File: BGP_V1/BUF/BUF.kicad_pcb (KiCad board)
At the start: 2 copper layers, 30 x 30 mm, 23 parts, among them P1 CONN_01X05, P2 CONN_01X02, P3 CONN_01X12, U1 MC33178, U2 TLV170

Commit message: BOM for V1 BGP
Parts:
- C2, C5: footprint Capacitors_SMD:C_1206_HandSoldering -> Capacitors_Tantalum_SMD:TantalC_SizeS_EIA-3216
- moved C5 0.22 mm to (162.4, 118.6), turned to 180 degrees
- moved C2 0.10 mm to (142.0, 107.6), turned to 0 degrees
- moved C6 0.10 mm to (150.4, 114.1)
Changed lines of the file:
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@@
   (general
     (links 49)
-    (no_connects 2)
-    (area 136.924999 91.924999 167.075001 122.075001)
+    (no_connects 0)
+    (area 135.10412 91.424999 167.075001 122.779999)
     (thickness 1.6)
     (drawings 9)
@@
     )
   )
-  (module Capacitors_SMD:C_1206_HandSoldering (layer F.Cu)
-    (at 142 107.5 180)
-    (descr "Capacitor SMD 1206, hand soldering")
-    (tags "capacitor 1206")
-    (attr smd)
-    (fp_text reference C2 (at 2.8 1.5 180) (layer F.SilkS)
-      (effects (font (size 0.6 0.6) (thickness 0.15)))
-    )
-    (fp_text value 10u (at 0 2.3 180) (layer F.Fab) hide
-      (effects (font (size 0.6 0.6) (thickness 0.15)))
-    )
-    (fp_line (start -3.3 -1.15) (end 3.3 -1.15) (layer F.CrtYd) (width 0.05))
-    (fp_line (start -3.3 1.15) (end 3.3 1.15) (layer F.CrtYd) (width 0.05))
-    (fp_line (start -3.3 -1.15) (end -3.3 1.15) (layer F.CrtYd) (width 0.05))
-    (fp_line (start 3.3 -1.15) (end 3.3 1.15) (layer F.CrtYd) (width 0.05))
-    (fp_line (start 1 -1.025) (end -1 -1.025) (layer F.SilkS) (width 0.15))
-    (fp_line (start -1 1.025) (end 1 1.025) (layer F.SilkS) (width 0.15))
-    (pad 1 smd rect (at -2 0 180) (size 2 1.6) (layers F.Cu F.Paste F.Mask)
-      (net 3 "Net-(C2-Pad1)"))
-    (pad 2 smd rect (at 2 0 180) (size 2 1.6) (layers F.Cu F.Paste F.Mask)
-      (net 18 /BUF_O))
-    (model Capacitors_SMD.3dshapes/C_1206_HandSoldering.wrl
-      (at (xyz 0 0 0))
-      (scale (xyz 1 1 1))
-      (rotate (xyz 0 0 0))
-    )
-  )
   (module Capacitors_SMD:C_0805_HandSoldering (layer F.Cu)
     (at 145.3 102.9 270)
@@
       (net 8 Earth))
     (model Capacitors_SMD.3dshapes/C_0805_HandSoldering.wrl
-      (at (xyz 0 0 0))
-      (scale (xyz 1 1 1))
-      (rotate (xyz 0 0 0))
-    )
-  )
-  (module Capacitors_SMD:C_1206_HandSoldering (layer F.Cu)
-    (at 162.5 118.4)
-    (descr "Capacitor SMD 1206, hand soldering")
-    (tags "capacitor 1206")
-    (attr smd)
-    (fp_text reference C5 (at -2.9 -1.6) (layer F.SilkS)
-      (effects (font (size 0.6 0.6) (thickness 0.15)))
-    )
-    (fp_text value 10u (at 0 2.3) (layer F.Fab) hide
-      (effects (font (size 0.6 0.6) (thickness 0.15)))
-    )
-    (fp_line (start -3.3 -1.15) (end 3.3 -1.15) (layer F.CrtYd) (width 0.05))
-    (fp_line (start -3.3 1.15) (end 3.3 1.15) (layer F.CrtYd) (width 0.05))
-    (fp_line (start -3.3 -1.15) (end -3.3 1.15) (layer F.CrtYd) (width 0.05))
-    (fp_line (start 3.3 -1.15) (end 3.3 1.15) (layer F.CrtYd) (width 0.05))
-    (fp_line (start 1 -1.025) (end -1 -1.025) (layer F.SilkS) (width 0.15))
-    (fp_line (start -1 1.025) (end 1 1.025) (layer F.SilkS) (width 0.15))
-    (pad 1 smd rect (at -2 0) (size 2 1.6) (layers F.Cu F.Paste F.Mask)
-      (net 9 /OUT))
-    (pad 2 smd rect (at 2 0) (size 2 1.6) (layers F.Cu F.Paste F.Mask)
-      (net 10 "Net-(C5-Pad2)"))
-    (model Capacitors_SMD.3dshapes/C_1206_HandSoldering.wrl
       (at (xyz 0 0 0))
       (scale (xyz 1 1 1))
@@
       (net 11 /V+))
     (model ${KISYS3DMOD}/TO_SOT_Packages_SMD.3dshapes\SOT-23-5.wrl
-      (at (xyz 0 0 0))
-      (scale (xyz 1 1 1))
-      (rotate (xyz 0 0 0))
-    )
-  )
-  (module Capacitors_SMD:C_0805_HandSoldering (layer B.Cu)
-    (at 150.3 114.1)
-    (descr "Capacitor SMD 0805, hand soldering")
-    (tags "capacitor 0805")
-    (attr smd)
-    (fp_text reference C6 (at 1.7 -1.3) (layer B.SilkS)
-      (effects (font (size 0.6 0.6) (thickness 0.15)) (justify mirror))
-    )
-    (fp_text value 10u (at 0 -1.75) (layer B.Fab) hide
-      (effects (font (size 0.6 0.6) (thickness 0.15)) (justify mirror))
-    )
-    (fp_text user %R (at 1.8 -1.4) (layer B.Fab) hide
-      (effects (font (size 0.6 0.6) (thickness 0.15)) (justify mirror))
-    )
-    (fp_line (start -1 -0.62) (end -1 0.62) (layer B.Fab) (width 0.1))
-    (fp_line (start 1 -0.62) (end -1 -0.62) (layer B.Fab) (width 0.1))
-    (fp_line (start 1 0.62) (end 1 -0.62) (layer B.Fab) (width 0.1))
-    (fp_line (start -1 0.62) (end 1 0.62) (layer B.Fab) (width 0.1))
-    (fp_line (start 0.5 0.85) (end -0.5 0.85) (layer B.SilkS) (width 0.12))
-    (fp_line (start -0.5 -0.85) (end 0.5 -0.85) (layer B.SilkS) (width 0.12))
-    (fp_line (start -2.25 0.88) (end 2.25 0.88) (layer B.CrtYd) (width 0.05))
-    (fp_line (start -2.25 0.88) (end -2.25 -0.87) (layer B.CrtYd) (width 0.05))
-    (fp_line (start 2.25 -0.87) (end 2.25 0.88) (layer B.CrtYd) (width 0.05))
-    (fp_line (start 2.25 -0.87) (end -2.25 -0.87) (layer B.CrtYd) (width 0.05))
-    (pad 1 smd rect (at -1.25 0) (size 1.5 1.25) (layers B.Cu B.Paste B.Mask)
-      (net 11 /V+))
-    (pad 2 smd rect (at 1.25 0) (size 1.5 1.25) (layers B.Cu B.Paste B.Mask)
-      (net 12 /V-))
-    (model Capacitors_SMD.3dshapes/C_0805.wrl
       (at (xyz 0 0 0))
       (scale (xyz 1 1 1))
@@
       (rotate (xyz 0 0 0))
     )
+  )
+  (module Capacitors_Tantalum_SMD:TantalC_SizeS_EIA-3216 (layer F.Cu)
+    (at 142 107.6)
+    (descr "Tantal Cap. , Size S, EIA-3216, Hand Soldering")
+    (fp_text reference C2 (at -2.1 -1.4) (layer F.SilkS)
+      (effects (font (size 0.6 0.6) (thickness 0.15)))
+    )
+    (fp_text value 10u (at 0 1.27) (layer F.Fab) hide
+      (effects (font (size 0.6 0.6) (thickness 0.15)))
+    )
+    (fp_line (start 1.143 0.8128) (end 1.143 -0.8128) (layer F.SilkS) (width 0.15))
+    (fp_line (start -1.6002 -0.8128) (end -1.6002 0.8128) (layer F.SilkS) (width 0.15))
+    (fp_line (start -1.6002 0.8128) (end 1.6002 0.8128) (layer F.SilkS) (width 0.15))
+    (fp_line (start 1.6002 0.8128) (end 1.6002 -0.8128) (layer F.SilkS) (width 0.15))
+    (fp_line (start 1.6002 -0.8128) (end -1.6002 -0.8128) (layer F.SilkS) (width 0.15))
+    (pad 1 smd rect (at 1.37414 0) (size 1.95072 1.50114) (layers F.Cu F.Paste F.Mask)
+      (net 3 "Net-(C2-Pad1)"))
+    (pad 2 smd rect (at -1.37414 0) (size 1.95072 1.50114) (layers F.Cu F.Paste F.Mask)
+      (net 18 /BUF_O))
+    (model Capacitors_Tantalum_SMD.3dshapes/TantalC_SizeS_EIA-3216.wrl
+      (at (xyz 0 0 0))
+      (scale (xyz 1 1 1))
+      (rotate (xyz 0 0 0))
+    )
+  )
+  (module Capacitors_Tantalum_SMD:TantalC_SizeS_EIA-3216 (layer F.Cu)
+    (at 162.4 118.6 180)
+    (descr "Tantal Cap. , Size S, EIA-3216, Hand Soldering")
+    (fp_text reference C5 (at 2.1 1.5 180) (layer F.SilkS)
+      (effects (font (size 0.6 0.6) (thickness 0.15)))
+    )
+    (fp_text value 10u (at 0 1.27 180) (layer F.Fab) hide
+      (effects (font (size 0.6 0.6) (thickness 0.15)))
+    )
+    (fp_line (start 1.143 0.8128) (end 1.143 -0.8128) (layer F.SilkS) (width 0.15))
+    (fp_line (start -1.6002 -0.8128) (end -1.6002 0.8128) (layer F.SilkS) (width 0.15))
+    (fp_line (start -1.6002 0.8128) (end 1.6002 0.8128) (layer F.SilkS) (width 0.15))
+    (fp_line (start 1.6002 0.8128) (end 1.6002 -0.8128) (layer F.SilkS) (width 0.15))
+    (fp_line (start 1.6002 -0.8128) (end -1.6002 -0.8128) (layer F.SilkS) (width 0.15))
+    (pad 1 smd rect (at 1.37414 0 180) (size 1.95072 1.50114) (layers F.Cu F.Paste F.Mask)
+      (net 9 /OUT))
+    (pad 2 smd rect (at -1.37414 0 180) (size 1.95072 1.50114) (layers F.Cu F.Paste F.Mask)
+      (net 10 "Net-(C5-Pad2)"))
+    (model Capacitors_Tantalum_SMD.3dshapes/TantalC_SizeS_EIA-3216.wrl
+      (at (xyz 0 0 0))
+      (scale (xyz 1 1 1))
+      (rotate (xyz 0 0 0))
+    )
+  )
+  (module Capacitors_SMD:C_0805_HandSoldering (layer B.Cu)
+    (at 150.4 114.1)
+    (descr "Capacitor SMD 0805, hand soldering")
+    (tags "capacitor 0805")
+    (attr smd)
+    (fp_text reference C6 (at 1.8 -1.4) (layer B.SilkS)
+      (effects (font (size 0.6 0.6) (thickness 0.15)) (justify mirror))
+    )
+    (fp_text value 10u (at 0 -2.1) (layer B.Fab) hide
+      (effects (font (size 0.6 0.6) (thickness 0.15)) (justify mirror))
+    )
+    (fp_line (start -2.3 1) (end 2.3 1) (layer B.CrtYd) (width 0.05))
+    (fp_line (start -2.3 -1) (end 2.3 -1) (layer B.CrtYd) (width 0.05))
+    (fp_line (start -2.3 1) (end -2.3 -1) (layer B.CrtYd) (width 0.05))
+    (fp_line (start 2.3 1) (end 2.3 -1) (layer B.CrtYd) (width 0.05))
+    (fp_line (start 0.5 0.85) (end -0.5 0.85) (layer B.SilkS) (width 0.15))
+    (fp_line (start -0.5 -0.85) (end 0.5 -0.85) (layer B.SilkS) (width 0.15))
+    (pad 1 smd rect (at -1.25 0) (size 1.5 1.25) (layers B.Cu B.Paste B.Mask)
+      (net 11 /V+))
+    (pad 2 smd rect (at 1.25 0) (size 1.5 1.25) (layers B.Cu B.Paste B.Mask)
+      (net 12 /V-))
+    (model Capacitors_SMD.3dshapes/C_0805_HandSoldering.wrl
+      (at (xyz 0 0 0))
+      (scale (xyz 1 1 1))
+      (rotate (xyz 0 0 0))
+    )

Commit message: some cleanup
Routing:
- net /VF2_2: track 12.8 -> 14.1 mm
- net Earth: track 10.1 -> 9.51 mm

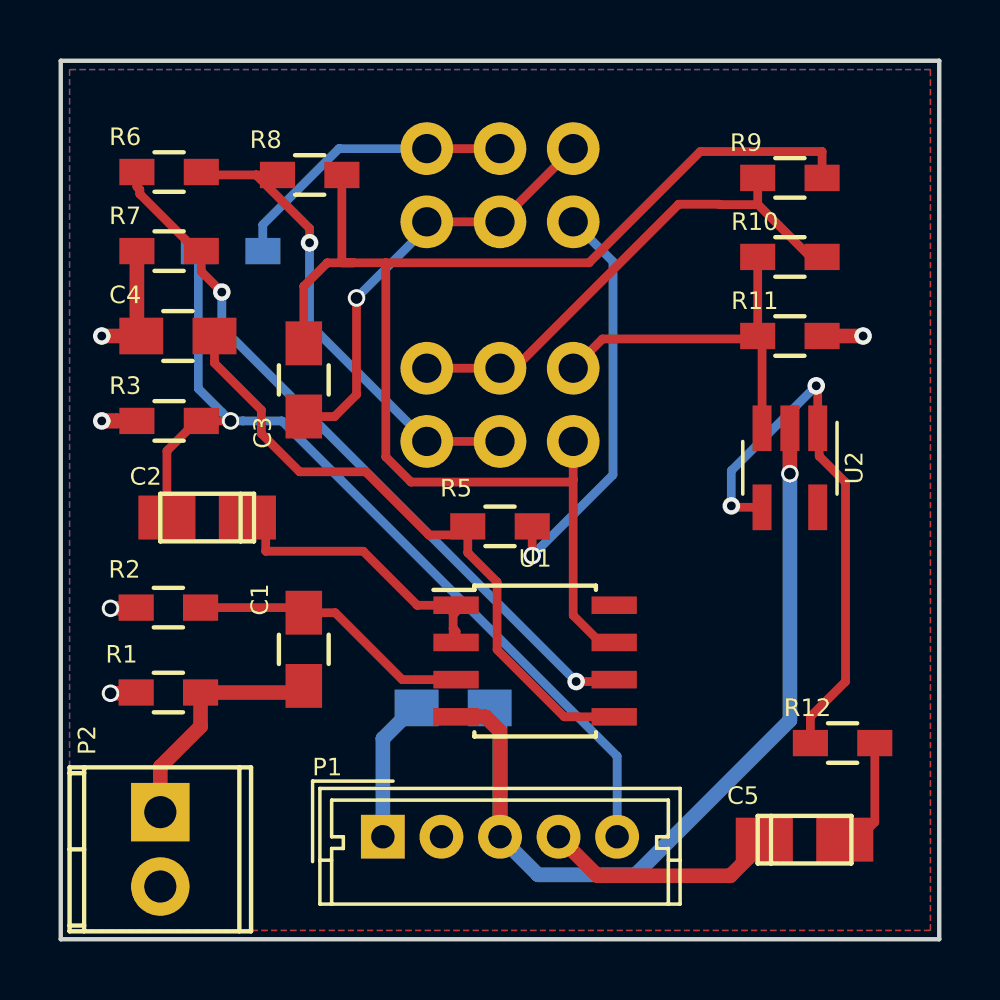
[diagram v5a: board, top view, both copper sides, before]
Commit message: Slight changes to Port layer placement - gerbers done
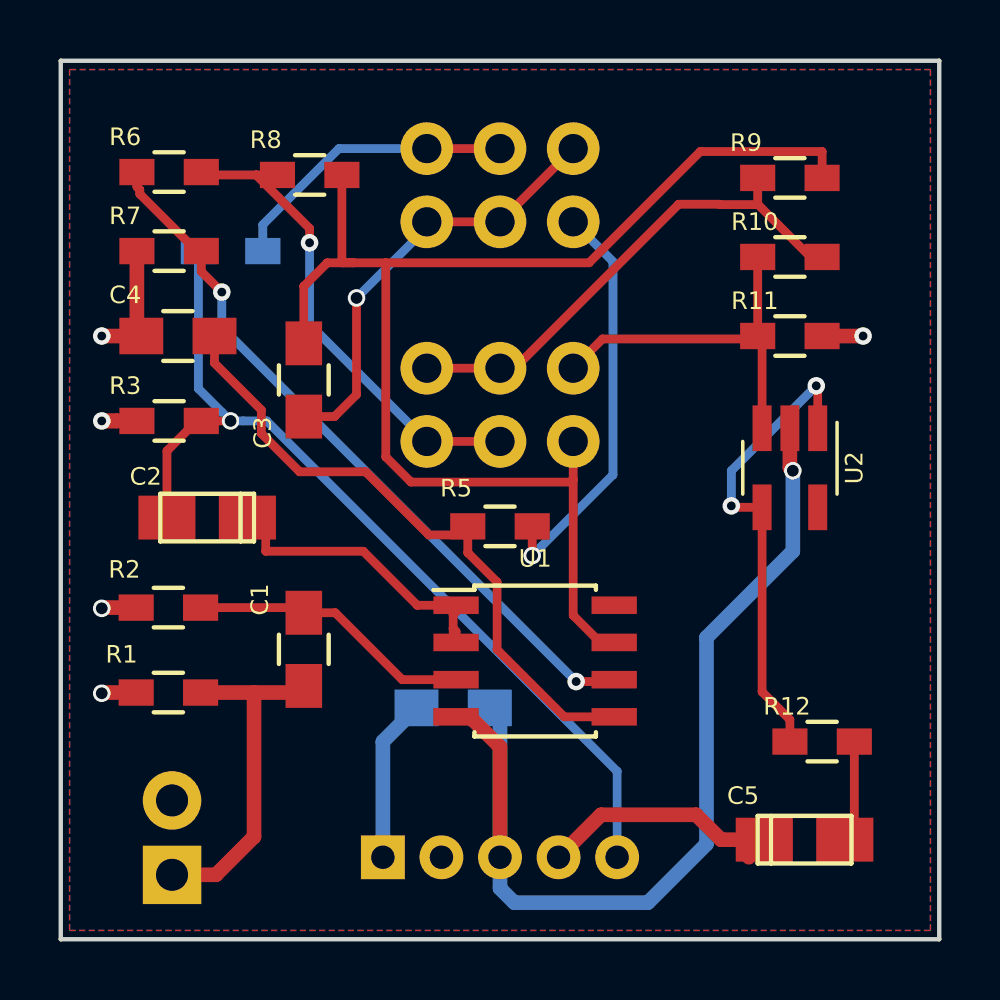
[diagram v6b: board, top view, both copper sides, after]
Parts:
- P1, P2: moved to B.Cu
- moved P2 2.18 mm to (140.8, 119.8), turned to 90 degrees
- moved R12 0.70 mm to (163.0, 115.2)
- moved P1 0.70 mm to (148.0, 119.2)
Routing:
- net /V-: track 32.6 -> 36.3 mm
- net /IN: track 8.47 -> 12.1 mm
- net Net-(R12-Pad2): track 19.5 -> 16.5 mm
- net /V+: track 4.83 -> 5.58 mm
- net /OUT: track 8.11 -> 8.78 mm
- net Earth: track 9.51 -> 10.1 mm
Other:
- board text added: "+"
- board text added: "-"
- board text added: "B"
- board text added: "G"
- board text added: "I"
- board text added: "O"

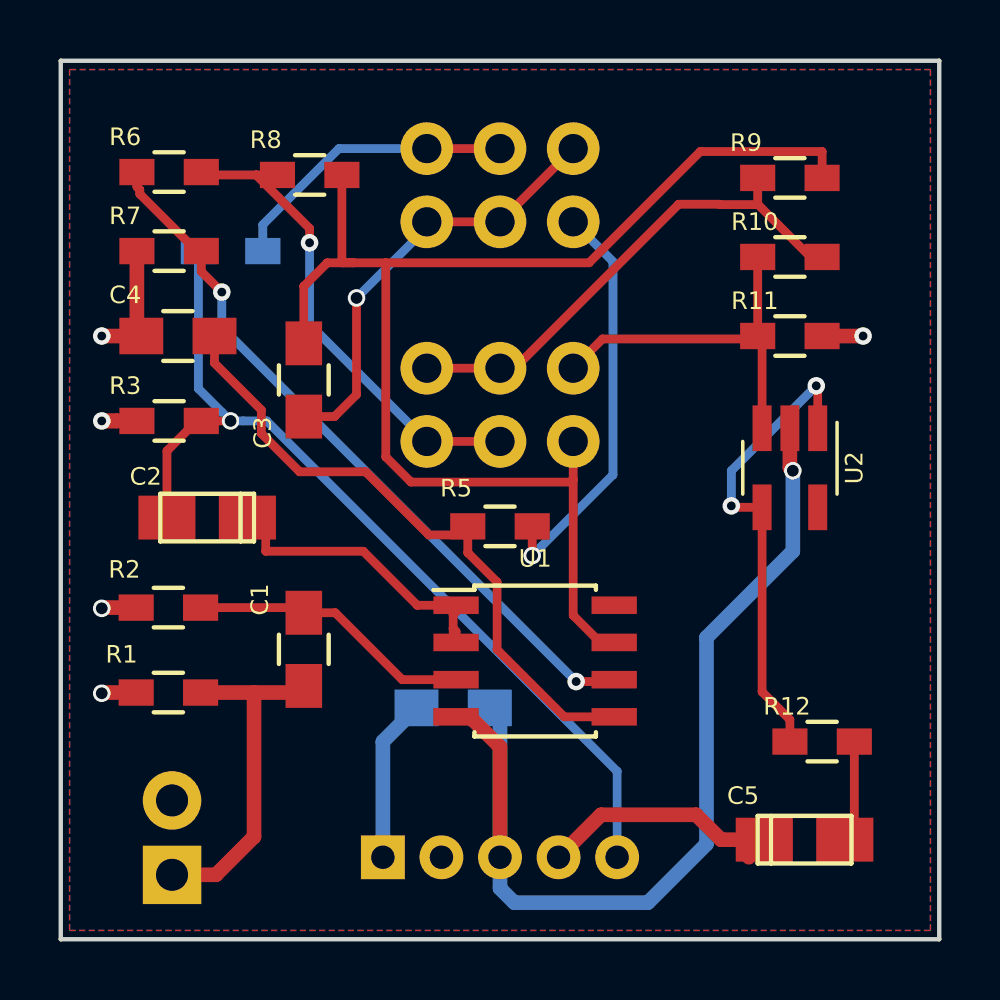
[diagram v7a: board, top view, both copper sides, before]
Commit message: Slight changes to Port layer placement - gerbers done
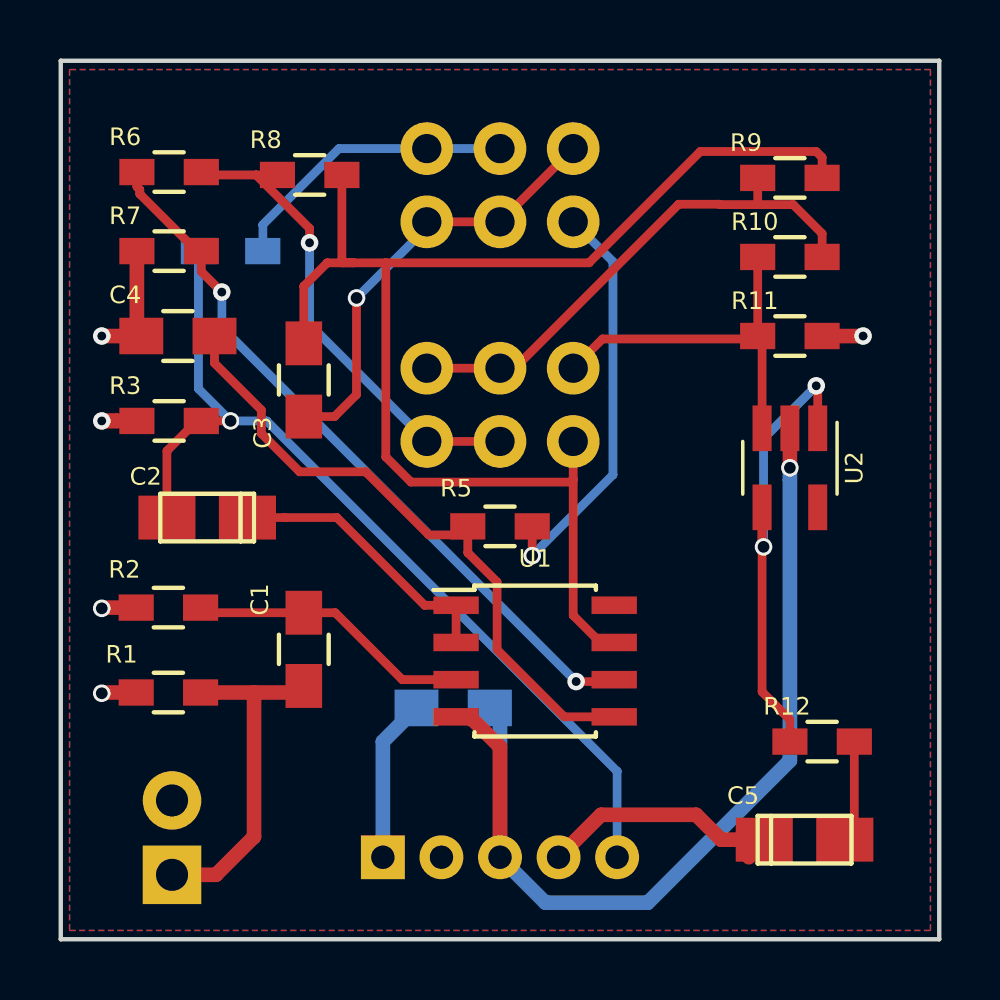
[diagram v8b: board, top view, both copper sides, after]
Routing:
- net Net-(R12-Pad2): track 16.5 -> 17.8 mm
- net Net-(C2-Pad1): track 10.6 -> 9.64 mm
- net /V-: track 36.3 -> 35.6 mm
